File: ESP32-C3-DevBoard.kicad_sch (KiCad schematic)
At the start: 21 parts, among them J1 USB_C_Receptacle_USB2.0, J2 Conn_01x10, J3 Conn_01x10, SW1 SW_Push, SW2 SW_Push, U1 ESP32-C3-WROOM-02, U3 RT9080-33GJ5

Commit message: Add files via upload
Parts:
- C3: value 100nF -> 1uF; LCSC C1525 -> C52923
- C4: value 100nF -> 0.1uF
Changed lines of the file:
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@@
       (effects (font (size 1.27 1.27)))
     )
-    (property "Value" "100nF" (at 137.16 48.26 90)
+    (property "Value" "0.1uF" (at 137.16 48.26 90)
       (effects (font (size 1.27 1.27)))
     )
@@
       (effects (font (size 1.27 1.27)))
     )
-    (property "Value" "100nF" (at 148.59 143.51 90)
+    (property "Value" "1uF" (at 148.59 143.51 90)
       (effects (font (size 1.27 1.27)))
     )
@@
       (effects (font (size 1.27 1.27)) hide)
     )
-    (property "Datasheet" "https://datasheet.lcsc.com/lcsc/1810191219_Samsung-Electro-Mechanics-CL05B104KO5NNNC_C1525.pdf" (at 148.59 147.32 0)
-      (effects (font (size 1.27 1.27)) hide)
-    )
-    (property "LCSC" "C1525" (at 148.59 147.32 90)
-      (effects (font (size 1.27 1.27)) hide)
-    )
+    (property "Datasheet" "https://datasheet.lcsc.com/lcsc/2304140030_Samsung-Electro-Mechanics-CL05A105KA5NQNC_C52923.pdf" (at 148.59 147.32 0)
+      (effects (font (size 1.27 1.27)) hide)
+    )
+    (property "LCSC" "C52923" (at 148.59 147.32 90)
+      (effects (font (size 1.27 1.27)) hide)
+    )

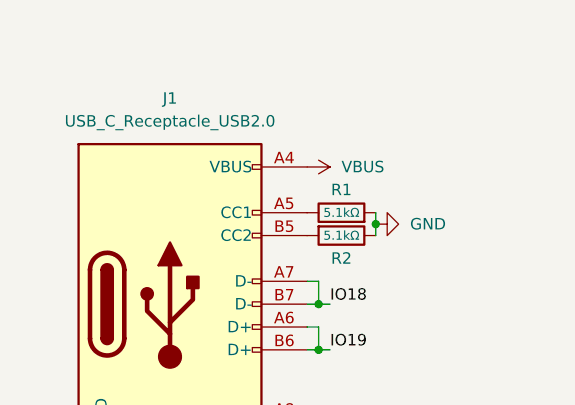
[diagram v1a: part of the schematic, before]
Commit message: KiCAD 8.0
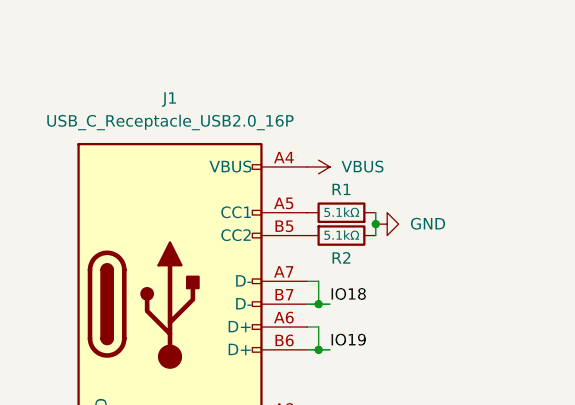
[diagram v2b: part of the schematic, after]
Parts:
- removed J1: USB_C_Receptacle_USB2.0, Connector_USB:USB_C_Receptacle_XKB_U262-16XN-4BVC11, symbol Connector:USB_C_Receptacle_USB2.0
- added J1: USB_C_Receptacle_USB2.0_16P, Connector_USB:USB_C_Receptacle_XKB_U262-16XN-4BVC11, symbol Connector:USB_C_Receptacle_USB2.0_16P
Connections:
- net GND: now also J1.A1 (GND), J1.A12 (GND), J1.B1 (GND), J1.B12 (GND), J1.S1 (SHIELD)
- net IO18: now also J1.A7 (D-), J1.B7 (D-)
- net IO19: now also J1.A6 (D+), J1.B6 (D+)
- net VBUS: now also J1.A4 (VBUS), J1.A9 (VBUS), J1.B4 (VBUS), J1.B9 (VBUS)
- net at R1.1: now also J1.A5 (CC1)
- net at R2.2: now also J1.B5 (CC2)

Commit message: Add files via upload
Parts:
- J1: JLCPCB Position Offset (none) -> 0, 1.27; LCSC (none) -> C2765186
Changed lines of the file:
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@@
+			)
+		)
+		(property "LCSC" "C2765186"
+			(at 64.77 76.2 0)
+			(effects
+				(font
+					(size 1.27 1.27)
+				)
+				(hide yes)
+			)
+		)
+		(property "JLCPCB Position Offset" "0, 1.27"
+			(at 64.77 76.2 0)
+			(effects
+				(font
+					(size 1.27 1.27)
+				)
+				(hide yes)
 			)
 		)
